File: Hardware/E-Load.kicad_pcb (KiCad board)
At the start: 2 copper layers, 76.2 x 71.1 mm, 115 parts, among them J1 PJ-002A, J2 Conn_01x05_Male, J3 Conn_01x08_Male, J4 Screw_Terminal_01x02, Q1 PSMN5R2-60YL, SW2 SW_Push, SW3 SW_Push, SW4 SW_Push, U1 AP2210K-3.3, U2 STM32F103C8Tx, U3 DAC121C081CIMK, U4 MCP6H04

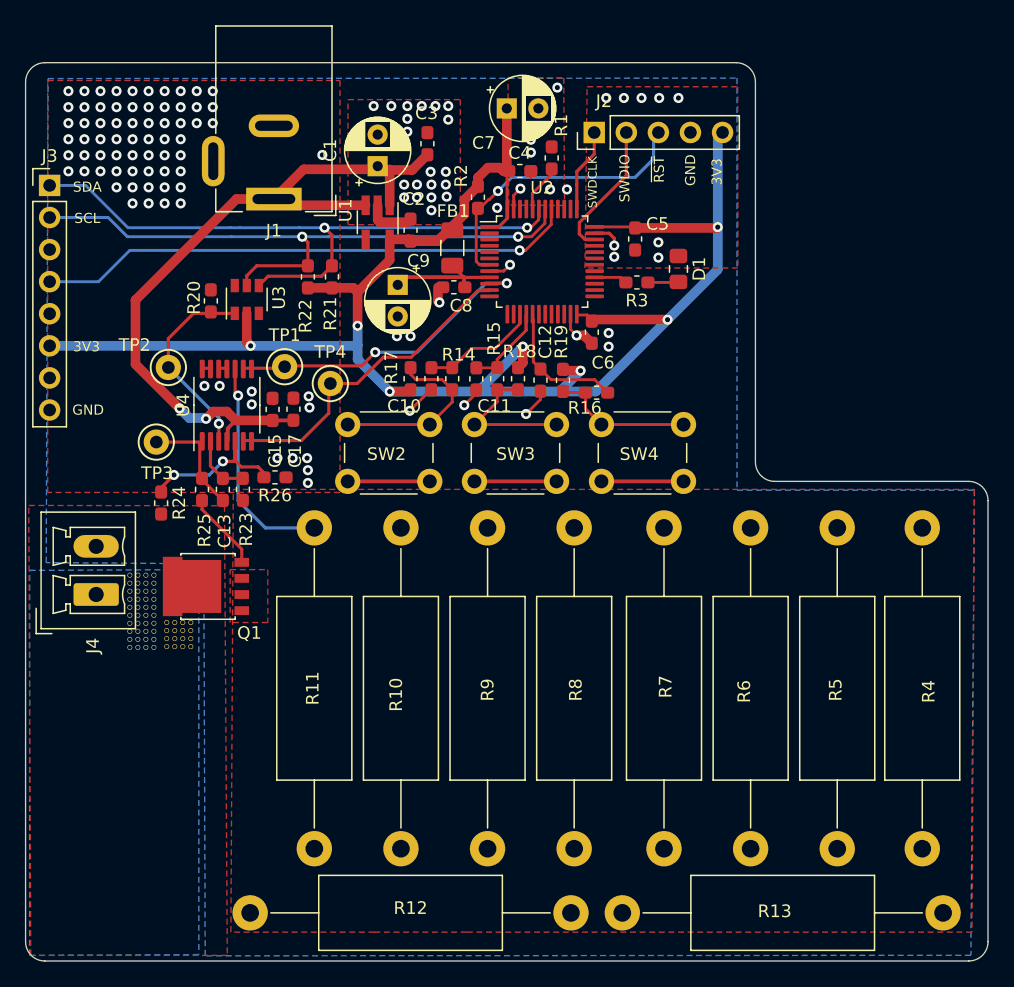
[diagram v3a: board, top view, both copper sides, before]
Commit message: Added second mosfet and added FPaste layer on thermal vias
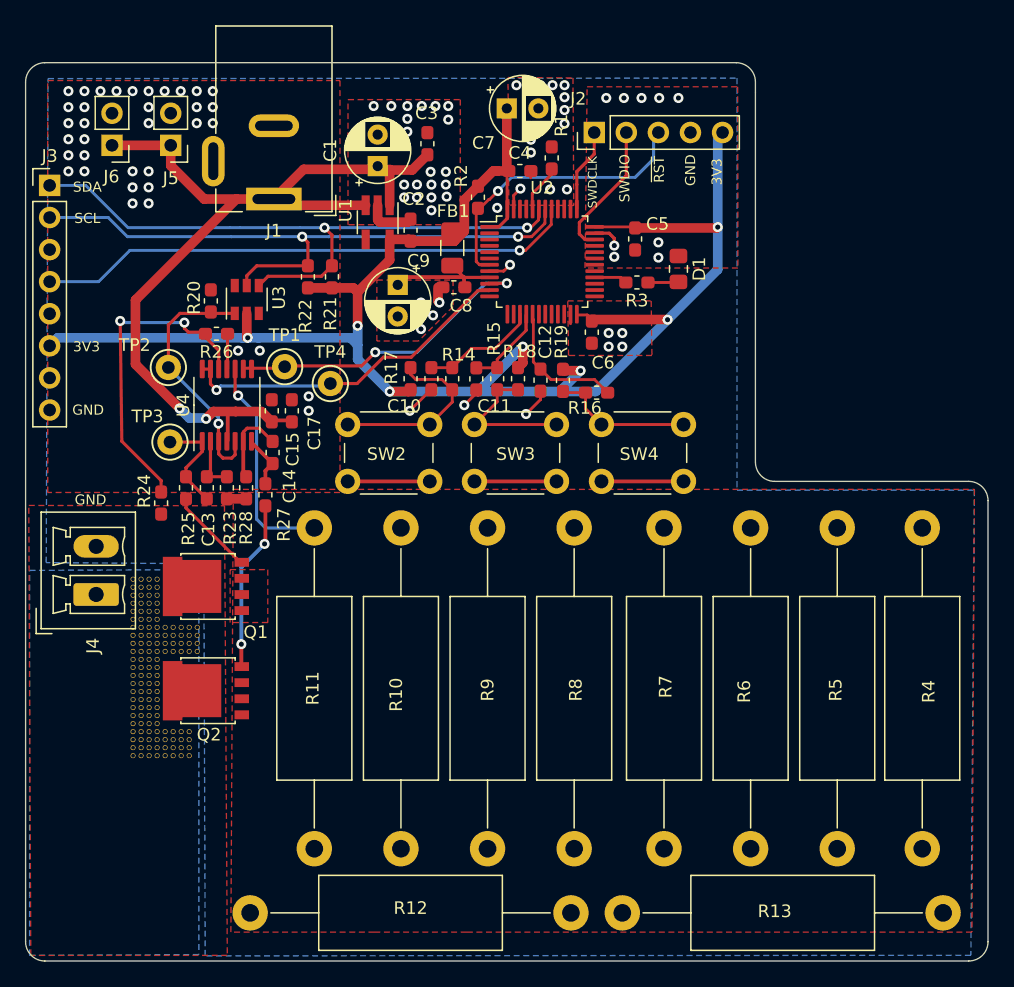
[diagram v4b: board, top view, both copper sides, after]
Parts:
- removed the REF** at (103.3, 108.5)
- removed the REF** at (105.2, 109.7)
- removed the REF** at (104.6, 109.7)
- removed the REF** at (103.9, 109.7)
- removed the REF** at (103.3, 109.7)
- removed the REF** at (105.2, 109.1)
- removed the REF** at (104.6, 109.1)
- removed the REF** at (103.9, 109.1)
- removed the REF** at (103.3, 109.1)
- removed the REF** at (105.2, 108.5)
- removed the REF** at (104.6, 108.5)
- removed the REF** at (105.2, 111.0)
- removed the REF** at (103.9, 108.5)
- removed the REF** at (105.2, 107.8)
- removed the REF** at (104.6, 107.8)
- removed the REF** at (103.9, 107.8)
- removed the REF** at (103.3, 107.8)
- removed the REF** at (105.2, 107.2)
- removed the REF** at (104.6, 107.2)
- removed the REF** at (103.9, 107.2)
- removed the REF** at (103.3, 107.2)
- removed the REF** at (105.2, 106.6)
- removed the REF** at (104.6, 111.0)
- removed the REF** at (104.6, 106.6)
- removed the REF** at (103.9, 106.6)
- removed the REF** at (103.3, 106.6)
- removed the REF** at (105.2, 105.9)
- removed the REF** at (104.6, 105.9)
- removed the REF** at (103.9, 105.9)
- removed the REF** at (103.3, 105.9)
- removed the REF** at (105.2, 105.3)
- removed the REF** at (104.6, 105.3)
- removed the REF** at (103.9, 105.3)
- removed the REF** at (103.9, 111.0)
- removed the REF** at (103.3, 105.3)
- removed the REF** at (108.1, 110.9)
- removed the REF** at (107.5, 110.9)
- removed the REF** at (106.9, 110.9)
- removed the REF** at (106.2, 110.9)
- removed the REF** at (108.1, 110.3)
- removed the REF** at (107.5, 110.3)
- removed the REF** at (106.9, 110.3)
- removed the REF** at (106.2, 110.3)
- removed the REF** at (108.1, 109.7)
- removed the REF** at (103.3, 111.0)
- removed the REF** at (107.5, 109.7)
- removed the REF** at (106.9, 109.7)
- removed the REF** at (106.2, 109.7)
- removed the REF** at (108.1, 109.0)
- removed the REF** at (107.5, 109.0)
- removed the REF** at (106.9, 109.0)
- removed the REF** at (106.2, 109.0)
- removed the REF** at (105.2, 110.4)
- removed the REF** at (104.6, 110.4)
- removed the REF** at (103.9, 110.4)
- removed the REF** at (103.3, 110.4)
- added C14: 470p, Capacitor_SMD:C_0603_1608Metric_Pad1.05x0.95mm_HandSolder, F.Cu at (114.6, 95.6)
- added J5: Conn_01x02_Male, Connector_PinHeader_2.54mm:PinHeader_1x02_P2.54mm_Vertical, F.Cu at (106.6, 71.2)
- added J6: Conn_01x02_Male, Connector_PinHeader_2.54mm:PinHeader_1x02_P2.54mm_Vertical, F.Cu at (101.9, 71.2)
- added Q2: PSMN5R2-60YL, Package_TO_SOT_SMD:LFPAK56, F.Cu at (109.3, 114.4)
- added R27: 75, Resistor_SMD:R_0603_1608Metric_Pad1.05x0.95mm_HandSolder, F.Cu at (114.0, 98.9)
- added R28: 1k, Resistor_SMD:R_0603_1608Metric_Pad1.05x0.95mm_HandSolder, F.Cu at (112.5, 98.4)
- added REF**: ThermalVia, ThermalVias:ThermalVia, F.Cu at (108.0, 119.6)
- added REF**: ThermalVia, ThermalVias:ThermalVia, F.Cu at (107.4, 118.3)
- added REF**: ThermalVia, ThermalVias:ThermalVia, F.Cu at (103.6, 110.0)
- added REF**: ThermalVia, ThermalVias:ThermalVia, F.Cu at (105.5, 109.4)
- added REF**: ThermalVia, ThermalVias:ThermalVia, F.Cu at (104.8, 109.4)
- added REF**: ThermalVia, ThermalVias:ThermalVia, F.Cu at (104.2, 109.4)
- added REF**: ThermalVia, ThermalVias:ThermalVia, F.Cu at (103.6, 109.4)
- added REF**: ThermalVia, ThermalVias:ThermalVia, F.Cu at (105.5, 108.8)
- added REF**: ThermalVia, ThermalVias:ThermalVia, F.Cu at (104.8, 108.8)
- added REF**: ThermalVia, ThermalVias:ThermalVia, F.Cu at (104.2, 108.8)
- added REF**: ThermalVia, ThermalVias:ThermalVia, F.Cu at (103.6, 108.8)
- added REF**: ThermalVia, ThermalVias:ThermalVia, F.Cu at (105.5, 108.1)
- added REF**: ThermalVia, ThermalVias:ThermalVia, F.Cu at (106.7, 118.3)
- added REF**: ThermalVia, ThermalVias:ThermalVia, F.Cu at (104.8, 108.1)
- added REF**: ThermalVia, ThermalVias:ThermalVia, F.Cu at (104.2, 108.1)
- added REF**: ThermalVia, ThermalVias:ThermalVia, F.Cu at (103.6, 108.1)
- added REF**: ThermalVia, ThermalVias:ThermalVia, F.Cu at (105.5, 107.5)
- added REF**: ThermalVia, ThermalVias:ThermalVia, F.Cu at (104.8, 107.5)
- added REF**: ThermalVia, ThermalVias:ThermalVia, F.Cu at (104.2, 107.5)
- added REF**: ThermalVia, ThermalVias:ThermalVia, F.Cu at (103.6, 107.5)
- added REF**: ThermalVia, ThermalVias:ThermalVia, F.Cu at (105.5, 106.9)
- added REF**: ThermalVia, ThermalVias:ThermalVia, F.Cu at (104.8, 106.9)
- added REF**: ThermalVia, ThermalVias:ThermalVia, F.Cu at (104.2, 106.9)
- added REF**: ThermalVia, ThermalVias:ThermalVia, F.Cu at (106.1, 118.3)
- added REF**: ThermalVia, ThermalVias:ThermalVia, F.Cu at (103.6, 106.9)
- added REF**: ThermalVia, ThermalVias:ThermalVia, F.Cu at (105.5, 106.2)
- added REF**: ThermalVia, ThermalVias:ThermalVia, F.Cu at (104.8, 106.2)
- added REF**: ThermalVia, ThermalVias:ThermalVia, F.Cu at (104.2, 106.2)
- added REF**: ThermalVia, ThermalVias:ThermalVia, F.Cu at (103.6, 106.2)
- added REF**: ThermalVia, ThermalVias:ThermalVia, F.Cu at (105.5, 105.6)
- added REF**: ThermalVia, ThermalVias:ThermalVia, F.Cu at (104.8, 105.6)
- added REF**: ThermalVia, ThermalVias:ThermalVia, F.Cu at (104.2, 105.6)
- added REF**: ThermalVia, ThermalVias:ThermalVia, F.Cu at (103.6, 105.6)
- added REF**: ThermalVia, ThermalVias:ThermalVia, F.Cu at (108.0, 117.7)
- added REF**: ThermalVia, ThermalVias:ThermalVia, F.Cu at (107.4, 117.7)
- added REF**: ThermalVia, ThermalVias:ThermalVia, F.Cu at (106.7, 117.7)
- added REF**: ThermalVia, ThermalVias:ThermalVia, F.Cu at (106.1, 117.7)
- added REF**: ThermalVia, ThermalVias:ThermalVia, F.Cu at (105.5, 119.6)
- added REF**: ThermalVia, ThermalVias:ThermalVia, F.Cu at (104.8, 119.6)
- added REF**: ThermalVia, ThermalVias:ThermalVia, F.Cu at (104.2, 119.6)
- added REF**: ThermalVia, ThermalVias:ThermalVia, F.Cu at (107.4, 119.6)
- added REF**: ThermalVia, ThermalVias:ThermalVia, F.Cu at (103.6, 119.6)
- added REF**: ThermalVia, ThermalVias:ThermalVia, F.Cu at (105.5, 118.9)
- added REF**: ThermalVia, ThermalVias:ThermalVia, F.Cu at (104.8, 118.9)
- added REF**: ThermalVia, ThermalVias:ThermalVia, F.Cu at (104.2, 118.9)
- added REF**: ThermalVia, ThermalVias:ThermalVia, F.Cu at (103.6, 118.9)
- added REF**: ThermalVia, ThermalVias:ThermalVia, F.Cu at (105.5, 118.3)
- added REF**: ThermalVia, ThermalVias:ThermalVia, F.Cu at (104.8, 118.3)
- added REF**: ThermalVia, ThermalVias:ThermalVia, F.Cu at (104.2, 118.3)
- added REF**: ThermalVia, ThermalVias:ThermalVia, F.Cu at (103.6, 118.3)
- added REF**: ThermalVia, ThermalVias:ThermalVia, F.Cu at (105.5, 117.7)
- added REF**: ThermalVia, ThermalVias:ThermalVia, F.Cu at (106.7, 119.6)
- added REF**: ThermalVia, ThermalVias:ThermalVia, F.Cu at (104.8, 117.7)
- added REF**: ThermalVia, ThermalVias:ThermalVia, F.Cu at (104.2, 117.7)
- added REF**: ThermalVia, ThermalVias:ThermalVia, F.Cu at (103.6, 117.7)
- added REF**: ThermalVia, ThermalVias:ThermalVia, F.Cu at (105.5, 117.0)
- added REF**: ThermalVia, ThermalVias:ThermalVia, F.Cu at (104.8, 117.0)
- added REF**: ThermalVia, ThermalVias:ThermalVia, F.Cu at (104.2, 117.0)
- added REF**: ThermalVia, ThermalVias:ThermalVia, F.Cu at (103.6, 117.0)
- added REF**: ThermalVia, ThermalVias:ThermalVia, F.Cu at (105.5, 116.4)
- added REF**: ThermalVia, ThermalVias:ThermalVia, F.Cu at (104.8, 116.4)
- added REF**: ThermalVia, ThermalVias:ThermalVia, F.Cu at (104.2, 116.4)
- added REF**: ThermalVia, ThermalVias:ThermalVia, F.Cu at (106.1, 119.6)
- added REF**: ThermalVia, ThermalVias:ThermalVia, F.Cu at (103.6, 116.4)
- added REF**: ThermalVia, ThermalVias:ThermalVia, F.Cu at (105.5, 115.8)
- added REF**: ThermalVia, ThermalVias:ThermalVia, F.Cu at (104.8, 115.8)
- added REF**: ThermalVia, ThermalVias:ThermalVia, F.Cu at (104.2, 115.8)
- added REF**: ThermalVia, ThermalVias:ThermalVia, F.Cu at (103.6, 115.8)
- added REF**: ThermalVia, ThermalVias:ThermalVia, F.Cu at (105.5, 115.1)
- added REF**: ThermalVia, ThermalVias:ThermalVia, F.Cu at (104.8, 115.1)
- added REF**: ThermalVia, ThermalVias:ThermalVia, F.Cu at (104.2, 115.1)
- added REF**: ThermalVia, ThermalVias:ThermalVia, F.Cu at (103.6, 115.1)
- added REF**: ThermalVia, ThermalVias:ThermalVia, F.Cu at (105.5, 114.5)
- added REF**: ThermalVia, ThermalVias:ThermalVia, F.Cu at (108.0, 118.9)
- added REF**: ThermalVia, ThermalVias:ThermalVia, F.Cu at (104.8, 114.5)
- added REF**: ThermalVia, ThermalVias:ThermalVia, F.Cu at (104.2, 114.5)
- added REF**: ThermalVia, ThermalVias:ThermalVia, F.Cu at (103.6, 114.5)
- added REF**: ThermalVia, ThermalVias:ThermalVia, F.Cu at (105.5, 113.9)
- added REF**: ThermalVia, ThermalVias:ThermalVia, F.Cu at (104.8, 113.9)
- added REF**: ThermalVia, ThermalVias:ThermalVia, F.Cu at (104.2, 113.9)
- added REF**: ThermalVia, ThermalVias:ThermalVia, F.Cu at (103.6, 113.9)
- added REF**: ThermalVia, ThermalVias:ThermalVia, F.Cu at (105.5, 113.2)
- added REF**: ThermalVia, ThermalVias:ThermalVia, F.Cu at (104.8, 113.2)
- added REF**: ThermalVia, ThermalVias:ThermalVia, F.Cu at (104.2, 113.2)
- added REF**: ThermalVia, ThermalVias:ThermalVia, F.Cu at (107.4, 118.9)
- added REF**: ThermalVia, ThermalVias:ThermalVia, F.Cu at (103.6, 113.2)
- added REF**: ThermalVia, ThermalVias:ThermalVia, F.Cu at (105.5, 112.6)
- added REF**: ThermalVia, ThermalVias:ThermalVia, F.Cu at (104.8, 112.6)
- added REF**: ThermalVia, ThermalVias:ThermalVia, F.Cu at (104.2, 112.6)
- added REF**: ThermalVia, ThermalVias:ThermalVia, F.Cu at (103.6, 112.6)
- added REF**: ThermalVia, ThermalVias:ThermalVia, F.Cu at (105.5, 112.0)
- added REF**: ThermalVia, ThermalVias:ThermalVia, F.Cu at (104.8, 112.0)
- added REF**: ThermalVia, ThermalVias:ThermalVia, F.Cu at (104.2, 112.0)
- added REF**: ThermalVia, ThermalVias:ThermalVia, F.Cu at (103.6, 112.0)
- added REF**: ThermalVia, ThermalVias:ThermalVia, F.Cu at (108.6, 111.3)
- added REF**: ThermalVia, ThermalVias:ThermalVia, F.Cu at (106.7, 118.9)
- added REF**: ThermalVia, ThermalVias:ThermalVia, F.Cu at (108.0, 111.3)
- added REF**: ThermalVia, ThermalVias:ThermalVia, F.Cu at (107.4, 111.3)
- added REF**: ThermalVia, ThermalVias:ThermalVia, F.Cu at (106.7, 111.3)
- added REF**: ThermalVia, ThermalVias:ThermalVia, F.Cu at (106.1, 111.3)
- added REF**: ThermalVia, ThermalVias:ThermalVia, F.Cu at (108.6, 110.7)
- added REF**: ThermalVia, ThermalVias:ThermalVia, F.Cu at (108.0, 110.7)
- added REF**: ThermalVia, ThermalVias:ThermalVia, F.Cu at (107.4, 110.7)
- added REF**: ThermalVia, ThermalVias:ThermalVia, F.Cu at (106.7, 110.7)
- added REF**: ThermalVia, ThermalVias:ThermalVia, F.Cu at (106.1, 110.7)
- added REF**: ThermalVia, ThermalVias:ThermalVia, F.Cu at (108.6, 110.0)
- added REF**: ThermalVia, ThermalVias:ThermalVia, F.Cu at (106.1, 118.9)
- added REF**: ThermalVia, ThermalVias:ThermalVia, F.Cu at (108.0, 110.0)
- added REF**: ThermalVia, ThermalVias:ThermalVia, F.Cu at (107.4, 110.0)
- added REF**: ThermalVia, ThermalVias:ThermalVia, F.Cu at (106.7, 110.0)
- added REF**: ThermalVia, ThermalVias:ThermalVia, F.Cu at (106.1, 110.0)
- added REF**: ThermalVia, ThermalVias:ThermalVia, F.Cu at (108.6, 109.4)
- added REF**: ThermalVia, ThermalVias:ThermalVia, F.Cu at (108.0, 109.4)
- added REF**: ThermalVia, ThermalVias:ThermalVia, F.Cu at (107.4, 109.4)
- added REF**: ThermalVia, ThermalVias:ThermalVia, F.Cu at (106.7, 109.4)
- added REF**: ThermalVia, ThermalVias:ThermalVia, F.Cu at (106.1, 109.4)
- added REF**: ThermalVia, ThermalVias:ThermalVia, F.Cu at (105.5, 111.3)
- added REF**: ThermalVia, ThermalVias:ThermalVia, F.Cu at (108.0, 118.3)
- added REF**: ThermalVia, ThermalVias:ThermalVia, F.Cu at (104.8, 111.3)
- added REF**: ThermalVia, ThermalVias:ThermalVia, F.Cu at (104.2, 111.3)
- added REF**: ThermalVia, ThermalVias:ThermalVia, F.Cu at (103.6, 111.3)
- added REF**: ThermalVia, ThermalVias:ThermalVia, F.Cu at (105.5, 110.7)
- added REF**: ThermalVia, ThermalVias:ThermalVia, F.Cu at (104.8, 110.7)
- added REF**: ThermalVia, ThermalVias:ThermalVia, F.Cu at (104.2, 110.7)
- added REF**: ThermalVia, ThermalVias:ThermalVia, F.Cu at (103.6, 110.7)
- added REF**: ThermalVia, ThermalVias:ThermalVia, F.Cu at (105.5, 110.0)
- added REF**: ThermalVia, ThermalVias:ThermalVia, F.Cu at (104.8, 110.0)
- added REF**: ThermalVia, ThermalVias:ThermalVia, F.Cu at (104.2, 110.0)
- C10: value 1u -> 1uF
- R14, R15, R16, R17, R18, R19: value 1K -> 1k
- moved R26 12.3 mm to (110.2, 86.2)
- moved C13 1.28 mm to (109.4, 98.4)
- moved R23 1.28 mm to (111.0, 98.4)
- moved R25 1.28 mm to (107.8, 98.4)
- moved TP3 1.08 mm to (106.5, 94.7)
- moved C17 0.18 mm to (116.1, 92.3)
- moved C15 0.13 mm to (114.6, 92.3)
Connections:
- U4 pad 12: GND -> Net-(R24-Pad1)
- U4 pad 13: Net-(U4-Pad13) -> /CurrentControl/Current_ADC
- U4 pad 14: Net-(U4-Pad13) -> /CurrentControl/Current_ADC
- U4 pad 5: Net-(R24-Pad1) -> Net-(R20-Pad2)
- U4 pad 6: /CurrentControl/Current_ADC -> Net-(C14-Pad2)
- U4 pad 7: /CurrentControl/Current_ADC -> Net-(C14-Pad1)
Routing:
- net +12V: track 60.9 -> 74.4 mm
- net Net-(R24-Pad1): track 12.4 -> 25.8 mm
- net Net-(Q2-Pad4): track 0.00 -> 13.4 mm, vias 0 -> 2
- net Net-(C14-Pad2): track 0.00 -> 6.84 mm
- net Net-(C14-Pad1): track 0.00 -> 4.29 mm
- net Net-(R20-Pad2): track 15.8 -> 20.1 mm
- net +3V3: track 146.6 -> 144.2 mm
- net /CurrentControl/Vmeas: track 17.4 -> 19.1 mm
- net /CurrentControl/Current_ADC: track 26.5 -> 27.4 mm, vias 0 -> 1
- net Net-(Q1-Pad4): track 6.20 -> 6.91 mm
- net Net-(U4-Pad13): track 0.65 -> 0.00 mm
- net Net-(C13-Pad1): track 9.18 -> 8.61 mm
- net GND: track 42.0 -> 41.7 mm, vias 121 -> 92
